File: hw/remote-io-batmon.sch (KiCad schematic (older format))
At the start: 0 parts

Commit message: Added ADC schematic and connections
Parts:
- added C?: C, symbol C
- added D2, D3, D4, D5, D6, D7, D8, D9: 3.9V, symbol ZENER
- added R10, R15, R16, R17, R18, R7, R8, R9: 11.3k, Resistors_SMD:R_0805_HandSoldering, symbol R
- added R11, R12, R13, R14, R3, R4, R5, R6: 78.7k, Resistors_SMD:R_0805_HandSoldering, symbol R
- added U2: MCP3008, symbol MCP3008
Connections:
- net labels added: +3.3V, ADC_CLK, ADC_DIN, ADC_DOUT, ADC_IN0, ADC_IN1, ADC_IN2, ADC_IN3, ADC_IN4, ADC_IN5, ADC_IN6, ADC_IN7, ADC_~CS~/SHDN, BAT_MEAS0, BAT_MEAS1, BAT_MEAS2, BAT_MEAS3, BAT_MEAS4, BAT_MEAS5, BAT_MEAS6, BAT_MEAS7, GNDA, GNDD
- wire segments 0 -> 51
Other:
- note added: "Over-Voltage Protected Inputs"
- note added: "SPI-Enabled ADC"

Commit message: Added I2C ID EEPROM
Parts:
- C3: renamed from C?; value C -> 0.1uF
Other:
- moved on the sheet: C3
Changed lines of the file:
@@
 $Descr USLetter 11000 8500
 encoding utf-8
-Sheet 3 3
+Sheet 3 4
 Title "Battery Monitor"
 Date "2015-06-15"
@@
 $EndComp
 $Comp
-L GNDA #PWR22
+L GNDA #PWR24
 U 1 1 557F5D8E
 P 6800 3200
-F 0 "#PWR22" H 6800 2950 50  0001 C CNN
+F 0 "#PWR24" H 6800 2950 50  0001 C CNN
 F 1 "GNDA" H 6800 3050 50  0000 C CNN
 F 2 "" H 6800 3200 60  0000 C CNN
@@
 ADC_IN0
 $Comp
-L GNDA #PWR26
+L GNDA #PWR28
 U 1 1 557FCB1A
 P 4350 4000
-F 0 "#PWR26" H 4350 3750 50  0001 C CNN
+F 0 "#PWR28" H 4350 3750 50  0001 C CNN
 F 1 "GNDA" H 4350 3850 50  0000 C CNN
 F 2 "" H 4350 4000 60  0000 C CNN
@@
 $EndComp
 $Comp
-L GNDD #PWR27
+L GNDD #PWR29
 U 1 1 557FCB60
 P 4600 4000
-F 0 "#PWR27" H 4600 3750 50  0001 C CNN
+F 0 "#PWR29" H 4600 3750 50  0001 C CNN
 F 1 "GNDD" H 4600 3850 50  0000 C CNN
 F 2 "" H 4600 4000 60  0000 C CNN
@@
 $EndComp
 $Comp
-L +3.3V #PWR21
+L +3.3V #PWR22
 U 1 1 557FCBFD
 P 4600 3100
-F 0 "#PWR21" H 4600 2950 50  0001 C CNN
+F 0 "#PWR22" H 4600 2950 50  0001 C CNN
 F 1 "+3.3V" H 4600 3240 50  0000 C CNN
 F 2 "" H 4600 3100 60  0000 C CNN
@@
 $EndComp
 $Comp
-L GNDA #PWR31
+L GNDA #PWR33
 U 1 1 557F806F
 P 8750 4600
-F 0 "#PWR31" H 8750 4350 50  0001 C CNN
+F 0 "#PWR33" H 8750 4350 50  0001 C CNN
 F 1 "GNDA" H 8750 4450 50  0000 C CNN
 F 2 "" H 8750 4600 60  0000 C CNN
@@
 $EndComp
 $Comp
-L GNDA #PWR30
+L GNDA #PWR32
 U 1 1 557F7CEF
 P 8100 4600
-F 0 "#PWR30" H 8100 4350 50  0001 C CNN
+F 0 "#PWR32" H 8100 4350 50  0001 C CNN
 F 1 "GNDA" H 8100 4450 50  0000 C CNN
 F 2 "" H 8100 4600 60  0000 C CNN
@@
 $EndComp
 $Comp
-L GNDA #PWR29
+L GNDA #PWR31
 U 1 1 557F7C36
 P 7450 4600
-F 0 "#PWR29" H 7450 4350 50  0001 C CNN
+F 0 "#PWR31" H 7450 4350 50  0001 C CNN
 F 1 "GNDA" H 7450 4450 50  0000 C CNN
 F 2 "" H 7450 4600 60  0000 C CNN
@@
 $EndComp
 $Comp
-L GNDA #PWR28
+L GNDA #PWR30
 U 1 1 557F7B9F
 P 6800 4600
-F 0 "#PWR28" H 6800 4350 50  0001 C CNN
+F 0 "#PWR30" H 6800 4350 50  0001 C CNN
 F 1 "GNDA" H 6800 4450 50  0000 C CNN
 F 2 "" H 6800 4600 60  0000 C CNN
@@
 $EndComp
 $Comp
-L GNDA #PWR24
+L GNDA #PWR26
 U 1 1 557F815E
 P 8100 3200
-F 0 "#PWR24" H 8100 2950 50  0001 C CNN
+F 0 "#PWR26" H 8100 2950 50  0001 C CNN
 F 1 "GNDA" H 8100 3050 50  0000 C CNN
 F 2 "" H 8100 3200 60  0000 C CNN
@@
 $EndComp
 $Comp
-L GNDA #PWR25
+L GNDA #PWR27
 U 1 1 557F7875
 P 8750 3200
-F 0 "#PWR25" H 8750 2950 50  0001 C CNN
+F 0 "#PWR27" H 8750 2950 50  0001 C CNN
 F 1 "GNDA" H 8750 3050 50  0000 C CNN
 F 2 "" H 8750 3200 60  0000 C CNN
@@
 $EndComp
 $Comp
-L GNDA #PWR23
+L GNDA #PWR25
 U 1 1 557F776F
 P 7450 3200
-F 0 "#PWR23" H 7450 2950 50  0001 C CNN
+F 0 "#PWR25" H 7450 2950 50  0001 C CNN
 F 1 "GNDA" H 7450 3050 50  0000 C CNN
 F 2 "" H 7450 3200 60  0000 C CNN
@@
 	4350 3900 4350 4000
 Wire Notes Line
-	3850 2650 3850 4400
+	3850 2600 3850 4350
 Wire Notes Line
 	3850 4400 6100 4400
 Wire Notes Line
-	6100 4400 6100 2650
-Wire Notes Line
-	6100 2650 3850 2650
+	6100 4400 6100 2600
+Wire Notes Line
+	6100 2600 3850 2600
 Wire Notes Line
 	6600 2200 6600 4900
@@
 Wire Notes Line
 	9400 2200 6600 2200
-Text Notes 3850 2650 0    60   ~ 0
+Text Notes 3850 2600 0    60   ~ 0
 SPI-Enabled ADC
 Text Notes 6600 2200 0    60   ~ 0
 Over-Voltage Protected Inputs
 $Comp
-L C C?
+L C C3
 U 1 1 558042F2
-P 4100 3050
-F 0 "C?" H 4125 3150 50  0000 L CNN
-F 1 "C" H 4125 2950 50  0000 L CNN
-F 2 "" H 4138 2900 30  0000 C CNN
-F 3 "" H 4100 3050 60  0000 C CNN
-	1    4100 3050
-	1    0    0    -1
-$EndComp
-$Comp
-L +3.3V #PWR?
+P 4100 3000
+F 0 "C3" H 4125 3100 50  0000 L CNN
+F 1 "0.1uF" H 4125 2900 50  0000 L CNN
+F 2 "" H 4138 2850 30  0000 C CNN
+F 3 "" H 4100 3000 60  0000 C CNN
+	1    4100 3000
+	1    0    0    -1
+$EndComp
+$Comp
+L +3.3V #PWR21
 U 1 1 55804385
-P 4100 2900
-F 0 "#PWR?" H 4100 2750 50  0001 C CNN
-F 1 "+3.3V" H 4100 3040 50  0000 C CNN
-F 2 "" H 4100 2900 60  0000 C CNN
-F 3 "" H 4100 2900 60  0000 C CNN
-	1    4100 2900
-	1    0    0    -1
-$EndComp
+P 4100 2850
+F 0 "#PWR21" H 4100 2700 50  0001 C CNN
+F 1 "+3.3V" H 4100 2990 50  0000 C CNN
+F 2 "" H 4100 2850 60  0000 C CNN
+F 3 "" H 4100 2850 60  0000 C CNN
+	1    4100 2850
+	1    0    0    -1
+$EndComp
+$Comp
+L GNDA #PWR23
+U 1 1 5581196F
+P 4100 3150
+F 0 "#PWR23" H 4100 2900 50  0001 C CNN
+F 1 "GNDA" H 4100 3000 50  0000 C CNN
+F 2 "" H 4100 3150 60  0000 C CNN
+F 3 "" H 4100 3150 60  0000 C CNN
+	1    4100 3150
+	1    0    0    -1
+$EndComp

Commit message: Matched all footprints to schem and created kicad_pcb file
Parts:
- C3: footprint (none) -> Capacitors_SMD:C_0805_HandSoldering
- D10: renamed from D6; footprint (none) -> Diodes_SMD:SOD-323
- D11: renamed from D7; footprint (none) -> Diodes_SMD:SOD-323
- D12: renamed from D8; footprint (none) -> Diodes_SMD:SOD-323
- D13: renamed from D9; footprint (none) -> Diodes_SMD:SOD-323
- D6: renamed from D2; footprint (none) -> Diodes_SMD:SOD-323
- D7: renamed from D3; footprint (none) -> Diodes_SMD:SOD-323
- D8: renamed from D4; footprint (none) -> Diodes_SMD:SOD-323
- D9: renamed from D5; footprint (none) -> Diodes_SMD:SOD-323
- U2: footprint (none) -> Housings_SOIC:SOIC-16_3.9x9.9mm_Pitch1.27mm
- renumbered R3 to R10, R4 to R11, R5 to R12, R6 to R13, R7 to R14, R8 to R15, R9 to R16, R10 to R17, R11 to R18, R12 to R19, R13 to R20, R14 to R21, R15 to R22, R16 to R23, R17 to R24, R18 to R25
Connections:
- net labels added: GND
- net labels removed: GNDA, GNDD
- wire segments 51 -> 42

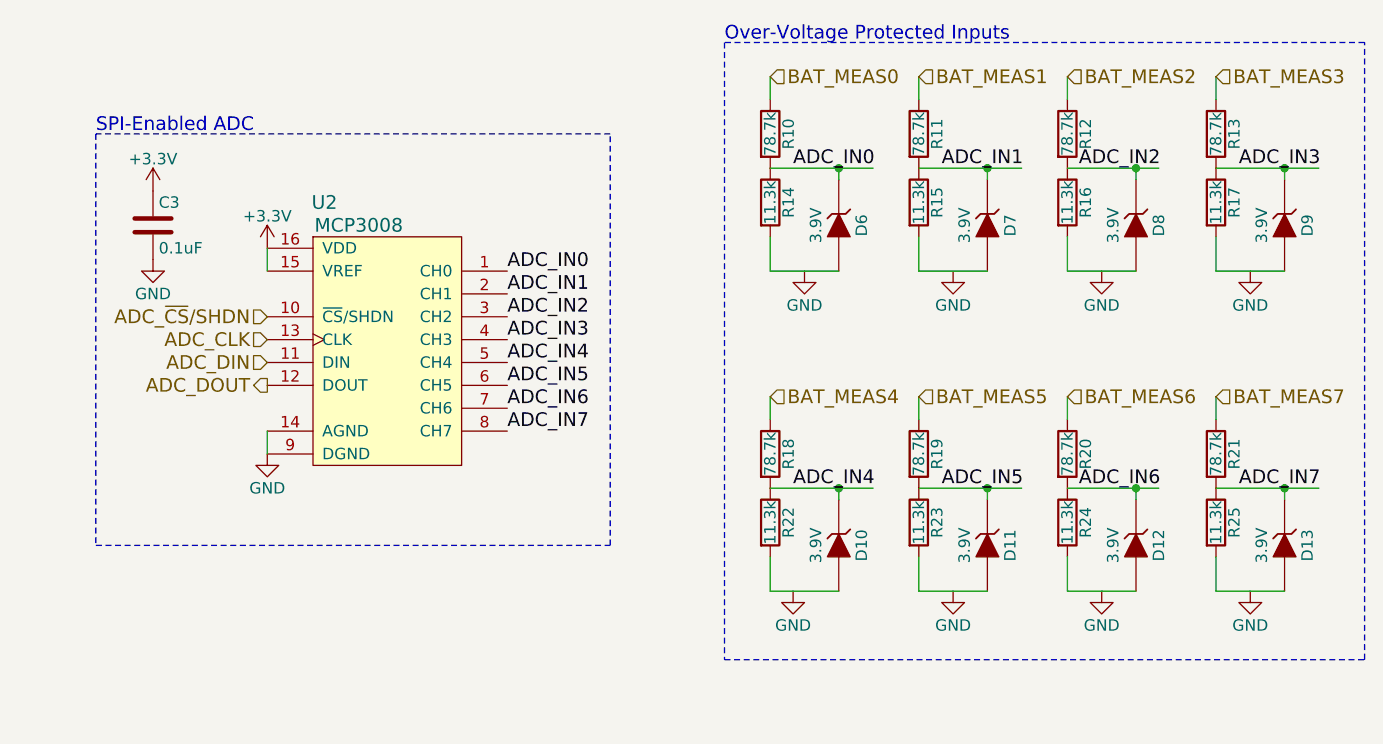
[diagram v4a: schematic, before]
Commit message: added CAN power, controller, and transceiver to schem and updated PCB
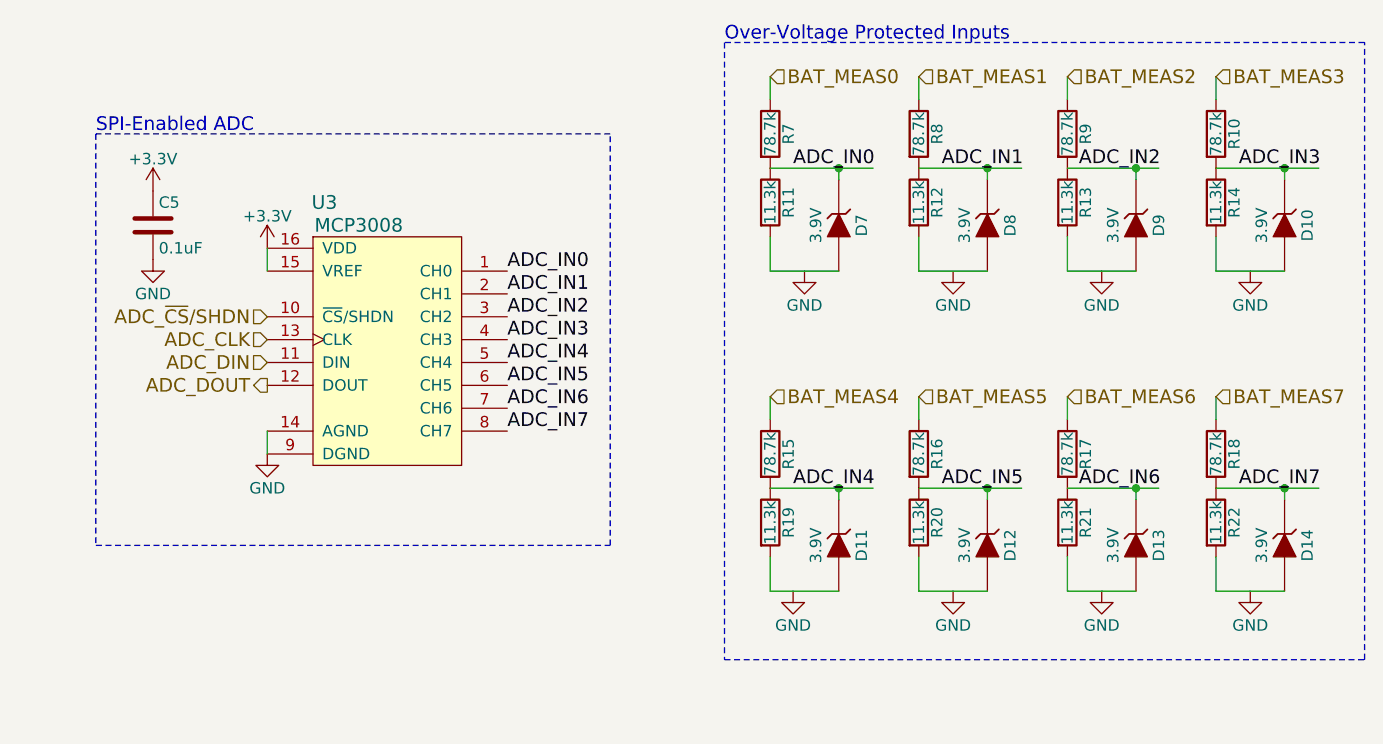
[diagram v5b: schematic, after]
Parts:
- renumbered C3 to C5, D9 to D10, D10 to D11, D11 to D12, D12 to D13, D13 to D14, D6 to D7, D7 to D8, D8 to D9, R13 to R10, R14 to R11, R15 to R12, R16 to R13, R17 to R14, R18 to R15, R19 to R16, R20 to R17, R21 to R18, R22 to R19, R23 to R20, R24 to R21, R25 to R22, R10 to R7, R11 to R8, R12 to R9, U2 to U3
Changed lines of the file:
@@
 $Descr USLetter 11000 8500
 encoding utf-8
-Sheet 3 5
+Sheet 3 6
 Title "Battery Monitor"
 Date "2015-06-15"
@@
 $EndDescr
 $Comp
-L MCP3008 U2
+L MCP3008 U3
 U 1 1 557F5C3F
 P 5100 3550
-F 0 "U2" H 4850 4200 60  0000 C CNN
+F 0 "U3" H 4850 4200 60  0000 C CNN
 F 1 "MCP3008" H 5000 4100 60  0000 C CNN
 F 2 "Housings_SOIC:SOIC-16_3.9x9.9mm_Pitch1.27mm" H 5100 3550 60  0001 C CNN
@@
 $EndComp
 $Comp
-L R R10
+L R R7
 U 1 1 557F5CD9
 P 6800 2600
-F 0 "R10" V 6880 2600 50  0000 C CNN
+F 0 "R7" V 6880 2600 50  0000 C CNN
 F 1 "78.7k" V 6800 2600 50  0000 C CNN
 F 2 "Resistors_SMD:R_0805_HandSoldering" V 6730 2600 30  0001 C CNN
@@
 $EndComp
 $Comp
-L R R14
+L R R11
 U 1 1 557F5D14
 P 6800 2900
-F 0 "R14" V 6880 2900 50  0000 C CNN
+F 0 "R11" V 6880 2900 50  0000 C CNN
 F 1 "11.3k" V 6800 2900 50  0000 C CNN
 F 2 "Resistors_SMD:R_0805_HandSoldering" V 6730 2900 30  0001 C CNN
@@
 $EndComp
 $Comp
-L ZENER D6
+L ZENER D7
 U 1 1 557F7000
 P 7100 3000
-F 0 "D6" H 7100 3100 50  0000 C CNN
+F 0 "D7" H 7100 3100 50  0000 C CNN
 F 1 "3.9V" H 7100 2900 50  0000 C CNN
 F 2 "Diodes_SMD:SOD-323" H 7100 3000 60  0001 C CNN
@@
 ADC_IN0
 $Comp
-L +3.3V #PWR033
+L +3.3V #PWR039
 U 1 1 557FCBFD
 P 4600 3100
-F 0 "#PWR033" H 4600 2950 50  0001 C CNN
+F 0 "#PWR039" H 4600 2950 50  0001 C CNN
 F 1 "+3.3V" H 4600 3240 50  0000 C CNN
 F 2 "" H 4600 3100 60  0000 C CNN
@@
 ADC_IN4
 $Comp
-L ZENER D13
+L ZENER D14
 U 1 1 557F8075
 P 9050 4400
-F 0 "D13" H 9050 4500 50  0000 C CNN
+F 0 "D14" H 9050 4500 50  0000 C CNN
 F 1 "3.9V" H 9050 4300 50  0000 C CNN
 F 2 "Diodes_SMD:SOD-323" H 9050 4400 60  0001 C CNN
@@
 $EndComp
 $Comp
-L ZENER D12
+L ZENER D13
 U 1 1 557F7CF5
 P 8400 4400
-F 0 "D12" H 8400 4500 50  0000 C CNN
+F 0 "D13" H 8400 4500 50  0000 C CNN
 F 1 "3.9V" H 8400 4300 50  0000 C CNN
 F 2 "Diodes_SMD:SOD-323" H 8400 4400 60  0001 C CNN
@@
 $EndComp
 $Comp
-L ZENER D11
+L ZENER D12
 U 1 1 557F7C3C
 P 7750 4400
-F 0 "D11" H 7750 4500 50  0000 C CNN
+F 0 "D12" H 7750 4500 50  0000 C CNN
 F 1 "3.9V" H 7750 4300 50  0000 C CNN
 F 2 "Diodes_SMD:SOD-323" H 7750 4400 60  0001 C CNN
@@
 $EndComp
 $Comp
-L ZENER D10
+L ZENER D11
 U 1 1 557F7BA5
 P 7100 4400
-F 0 "D10" H 7100 4500 50  0000 C CNN
+F 0 "D11" H 7100 4500 50  0000 C CNN
 F 1 "3.9V" H 7100 4300 50  0000 C CNN
 F 2 "Diodes_SMD:SOD-323" H 7100 4400 60  0001 C CNN
@@
 ADC_IN7
 $Comp
-L R R25
+L R R22
 U 1 1 557F67DD
 P 8750 4300
-F 0 "R25" V 8830 4300 50  0000 C CNN
+F 0 "R22" V 8830 4300 50  0000 C CNN
 F 1 "11.3k" V 8750 4300 50  0000 C CNN
 F 2 "Resistors_SMD:R_0805_HandSoldering" V 8680 4300 30  0001 C CNN
@@
 $EndComp
 $Comp
-L R R21
+L R R18
 U 1 1 557F67D7
 P 8750 4000
-F 0 "R21" V 8830 4000 50  0000 C CNN
+F 0 "R18" V 8830 4000 50  0000 C CNN
 F 1 "78.7k" V 8750 4000 50  0000 C CNN
 F 2 "Resistors_SMD:R_0805_HandSoldering" V 8680 4000 30  0001 C CNN
@@
 $EndComp
 $Comp
-L R R24
+L R R21
 U 1 1 557F67C6
 P 8100 4300
-F 0 "R24" V 8180 4300 50  0000 C CNN
+F 0 "R21" V 8180 4300 50  0000 C CNN
 F 1 "11.3k" V 8100 4300 50  0000 C CNN
 F 2 "Resistors_SMD:R_0805_HandSoldering" V 8030 4300 30  0001 C CNN
@@
 $EndComp
 $Comp
-L R R20
+L R R17
 U 1 1 557F67C0
 P 8100 4000
-F 0 "R20" V 8180 4000 50  0000 C CNN
+F 0 "R17" V 8180 4000 50  0000 C CNN
 F 1 "78.7k" V 8100 4000 50  0000 C CNN
 F 2 "Resistors_SMD:R_0805_HandSoldering" V 8030 4000 30  0001 C CNN
@@
 $EndComp
 $Comp
-L R R23
+L R R20
 U 1 1 557F67AF
 P 7450 4300
-F 0 "R23" V 7530 4300 50  0000 C CNN
+F 0 "R20" V 7530 4300 50  0000 C CNN
 F 1 "11.3k" V 7450 4300 50  0000 C CNN
 F 2 "Resistors_SMD:R_0805_HandSoldering" V 7380 4300 30  0001 C CNN
@@
 $EndComp
 $Comp
-L R R19
+L R R16
 U 1 1 557F67A9
 P 7450 4000
-F 0 "R19" V 7530 4000 50  0000 C CNN
+F 0 "R16" V 7530 4000 50  0000 C CNN
 F 1 "78.7k" V 7450 4000 50  0000 C CNN
 F 2 "Resistors_SMD:R_0805_HandSoldering" V 7380 4000 30  0001 C CNN
@@
 $EndComp
 $Comp
-L R R22
+L R R19
 U 1 1 557F6798
 P 6800 4300
-F 0 "R22" V 6880 4300 50  0000 C CNN
+F 0 "R19" V 6880 4300 50  0000 C CNN
 F 1 "11.3k" V 6800 4300 50  0000 C CNN
 F 2 "Resistors_SMD:R_0805_HandSoldering" V 6730 4300 30  0001 C CNN
@@
 $EndComp
 $Comp
-L R R18
+L R R15
 U 1 1 557F6792
 P 6800 4000
-F 0 "R18" V 6880 4000 50  0000 C CNN
+F 0 "R15" V 6880 4000 50  0000 C CNN
 F 1 "78.7k" V 6800 4000 50  0000 C CNN
 F 2 "Resistors_SMD:R_0805_HandSoldering" V 6730 4000 30  0001 C CNN
@@
 ADC_IN1
 $Comp
-L ZENER D8
+L ZENER D9
 U 1 1 557F8164
 P 8400 3000
-F 0 "D8" H 8400 3100 50  0000 C CNN
+F 0 "D9" H 8400 3100 50  0000 C CNN
 F 1 "3.9V" H 8400 2900 50  0000 C CNN
 F 2 "Diodes_SMD:SOD-323" H 8400 3000 60  0001 C CNN
@@
 $EndComp
 $Comp
-L ZENER D9
+L ZENER D10
 U 1 1 557F787B
 P 9050 3000
-F 0 "D9" H 9050 3100 50  0000 C CNN
+F 0 "D10" H 9050 3100 50  0000 C CNN
 F 1 "3.9V" H 9050 2900 50  0000 C CNN
 F 2 "Diodes_SMD:SOD-323" H 9050 3000 60  0001 C CNN
@@
 $EndComp
 $Comp
-L ZENER D7
+L ZENER D8
 U 1 1 557F7775
 P 7750 3000
-F 0 "D7" H 7750 3100 50  0000 C CNN
+F 0 "D8" H 7750 3100 50  0000 C CNN
 F 1 "3.9V" H 7750 2900 50  0000 C CNN
 F 2 "Diodes_SMD:SOD-323" H 7750 3000 60  0001 C CNN
@@
 $EndComp
 $Comp
-L R R17
+L R R14
 U 1 1 557F64CF
 P 8750 2900
-F 0 "R17" V 8830 2900 50  0000 C CNN
+F 0 "R14" V 8830 2900 50  0000 C CNN
 F 1 "11.3k" V 8750 2900 50  0000 C CNN
 F 2 "Resistors_SMD:R_0805_HandSoldering" V 8680 2900 30  0001 C CNN
@@
 $EndComp
 $Comp
-L R R13
+L R R10
 U 1 1 557F64C9
 P 8750 2600
-F 0 "R13" V 8830 2600 50  0000 C CNN
+F 0 "R10" V 8830 2600 50  0000 C CNN
 F 1 "78.7k" V 8750 2600 50  0000 C CNN
 F 2 "Resistors_SMD:R_0805_HandSoldering" V 8680 2600 30  0001 C CNN
@@
 $EndComp
 $Comp
-L R R16
+L R R13
 U 1 1 557F64B8
 P 8100 2900
-F 0 "R16" V 8180 2900 50  0000 C CNN
+F 0 "R13" V 8180 2900 50  0000 C CNN
 F 1 "11.3k" V 8100 2900 50  0000 C CNN
 F 2 "Resistors_SMD:R_0805_HandSoldering" V 8030 2900 30  0001 C CNN
@@
 $EndComp
 $Comp
-L R R12
+L R R9
 U 1 1 557F64B2
 P 8100 2600
-F 0 "R12" V 8180 2600 50  0000 C CNN
+F 0 "R9" V 8180 2600 50  0000 C CNN
 F 1 "78.7k" V 8100 2600 50  0000 C CNN
 F 2 "Resistors_SMD:R_0805_HandSoldering" V 8030 2600 30  0001 C CNN
@@
 $EndComp
 $Comp
-L R R15
+L R R12
 U 1 1 557F617C
 P 7450 2900
-F 0 "R15" V 7530 2900 50  0000 C CNN
+F 0 "R12" V 7530 2900 50  0000 C CNN
 F 1 "11.3k" V 7450 2900 50  0000 C CNN
 F 2 "Resistors_SMD:R_0805_HandSoldering" V 7380 2900 30  0001 C CNN
@@
 $EndComp
 $Comp
-L R R11
+L R R8
 U 1 1 557F6176
 P 7450 2600
-F 0 "R11" V 7530 2600 50  0000 C CNN
+F 0 "R8" V 7530 2600 50  0000 C CNN
 F 1 "78.7k" V 7450 2600 50  0000 C CNN
 F 2 "Resistors_SMD:R_0805_HandSoldering" V 7380 2600 30  0001 C CNN
@@
 Over-Voltage Protected Inputs
 $Comp
-L C C3
+L C C5
 U 1 1 558042F2
 P 4100 3000
-F 0 "C3" H 4125 3100 50  0000 L CNN
+F 0 "C5" H 4125 3100 50  0000 L CNN
 F 1 "0.1uF" H 4125 2900 50  0000 L CNN
 F 2 "Capacitors_SMD:C_0805_HandSoldering" H 4138 2850 30  0001 C CNN
@@
 $EndComp
 $Comp
-L +3.3V #PWR034
+L +3.3V #PWR040
 U 1 1 55804385
 P 4100 2850
-F 0 "#PWR034" H 4100 2700 50  0001 C CNN
+F 0 "#PWR040" H 4100 2700 50  0001 C CNN
 F 1 "+3.3V" H 4100 2990 50  0000 C CNN
 F 2 "" H 4100 2850 60  0000 C CNN
@@
 	4600 3900 4600 4000
 $Comp
-L GND #PWR035
+L GND #PWR041
 U 1 1 5582E9BE
 P 4600 4000
-F 0 "#PWR035" H 4600 3750 50  0001 C CNN
+F 0 "#PWR041" H 4600 3750 50  0001 C CNN
 F 1 "GND" H 4600 3850 50  0000 C CNN
 F 2 "" H 4600 4000 60  0000 C CNN
@@
 $EndComp
 $Comp
-L GND #PWR036
+L GND #PWR042
 U 1 1 5582EA8B
 P 4100 3150
-F 0 "#PWR036" H 4100 2900 50  0001 C CNN
+F 0 "#PWR042" H 4100 2900 50  0001 C CNN
 F 1 "GND" H 4100 3000 50  0000 C CNN
 F 2 "" H 4100 3150 60  0000 C CNN
@@
 $EndComp
 $Comp
-L GND #PWR037
+L GND #PWR043
 U 1 1 5582EDB2
 P 6950 3200
-F 0 "#PWR037" H 6950 2950 50  0001 C CNN
+F 0 "#PWR043" H 6950 2950 50  0001 C CNN
 F 1 "GND" H 6950 3050 50  0000 C CNN
 F 2 "" H 6950 3200 60  0000 C CNN
@@
 $EndComp
 $Comp
-L GND #PWR038
+L GND #PWR044
 U 1 1 5582EE12
 P 7600 3200
-F 0 "#PWR038" H 7600 2950 50  0001 C CNN
+F 0 "#PWR044" H 7600 2950 50  0001 C CNN
 F 1 "GND" H 7600 3050 50  0000 C CNN
 F 2 "" H 7600 3200 60  0000 C CNN
@@
 $EndComp
 $Comp
-L GND #PWR039
+L GND #PWR045
 U 1 1 5582EE51
 P 8250 3200
-F 0 "#PWR039" H 8250 2950 50  0001 C CNN
+F 0 "#PWR045" H 8250 2950 50  0001 C CNN
 F 1 "GND" H 8250 3050 50  0000 C CNN
 F 2 "" H 8250 3200 60  0000 C CNN
@@
 $EndComp
 $Comp
-L GND #PWR040
+L GND #PWR046
 U 1 1 5582EE95
 P 8900 3200
-F 0 "#PWR040" H 8900 2950 50  0001 C CNN
+F 0 "#PWR046" H 8900 2950 50  0001 C CNN
 F 1 "GND" H 8900 3050 50  0000 C CNN
 F 2 "" H 8900 3200 60  0000 C CNN
@@
 $EndComp
 $Comp
-L GND #PWR041
+L GND #PWR047
 U 1 1 5582EED9
 P 8900 4600
-F 0 "#PWR041" H 8900 4350 50  0001 C CNN
+F 0 "#PWR047" H 8900 4350 50  0001 C CNN
 F 1 "GND" H 8900 4450 50  0000 C CNN
 F 2 "" H 8900 4600 60  0000 C CNN
@@
 $EndComp
 $Comp
-L GND #PWR042
+L GND #PWR048
 U 1 1 5582EF1D
 P 8250 4600
-F 0 "#PWR042" H 8250 4350 50  0001 C CNN
+F 0 "#PWR048" H 8250 4350 50  0001 C CNN
 F 1 "GND" H 8250 4450 50  0000 C CNN
 F 2 "" H 8250 4600 60  0000 C CNN
@@
 $EndComp
 $Comp
-L GND #PWR043
+L GND #PWR049
 U 1 1 5582EF61
 P 7600 4600
-F 0 "#PWR043" H 7600 4350 50  0001 C CNN
+F 0 "#PWR049" H 7600 4350 50  0001 C CNN
 F 1 "GND" H 7600 4450 50  0000 C CNN
 F 2 "" H 7600 4600 60  0000 C CNN
@@
 $EndComp
 $Comp
-L GND #PWR044
+L GND #PWR050
 U 1 1 5582EFA5
 P 6900 4600
-F 0 "#PWR044" H 6900 4350 50  0001 C CNN
+F 0 "#PWR050" H 6900 4350 50  0001 C CNN
 F 1 "GND" H 6900 4450 50  0000 C CNN
 F 2 "" H 6900 4600 60  0000 C CNN

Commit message: Started fucking aroond with pcb layout. Power is tricky...
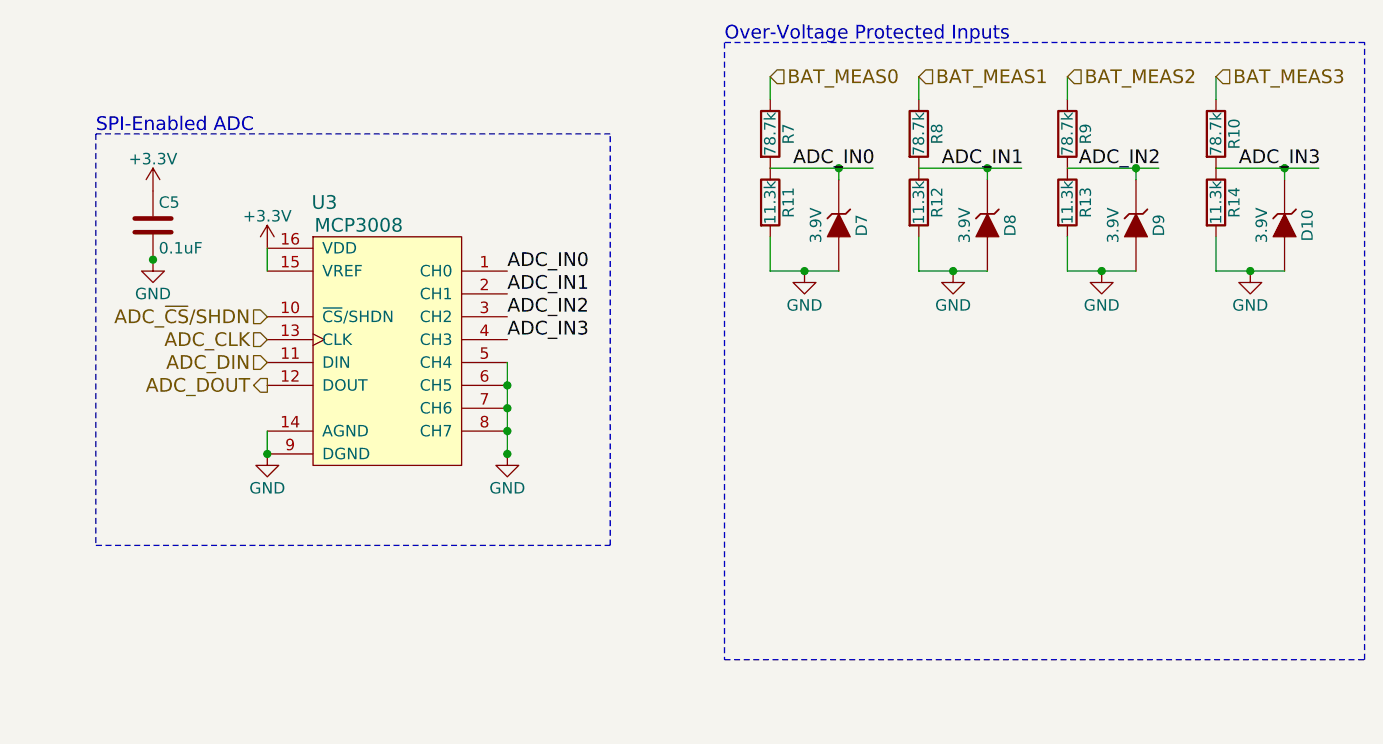
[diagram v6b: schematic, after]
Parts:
- removed D11, D12, D13, D14: 3.9V, Diodes_SMD:SOD-323, symbol ZENER
- removed R15, R16, R17, R18: 78.7k, Resistors_SMD:R_0805_HandSoldering, symbol R
- removed R19, R20, R21, R22: 11.3k, Resistors_SMD:R_0805_HandSoldering, symbol R
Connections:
- net labels removed: ADC_IN4, ADC_IN5, ADC_IN6, ADC_IN7, BAT_MEAS4, BAT_MEAS5, BAT_MEAS6, BAT_MEAS7
- wire segments 42 -> 23
